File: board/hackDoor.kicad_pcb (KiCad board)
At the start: 2 copper layers, 66 x 34.5 mm, 11 parts, among them P1 RFID Reader, P2 Lock Button, P3 Lock/Unlock, P4 RFID Reader, P5 Lock Button, Q1 BSS138, SW1 SW_PUSH, U1 RFID-ID12

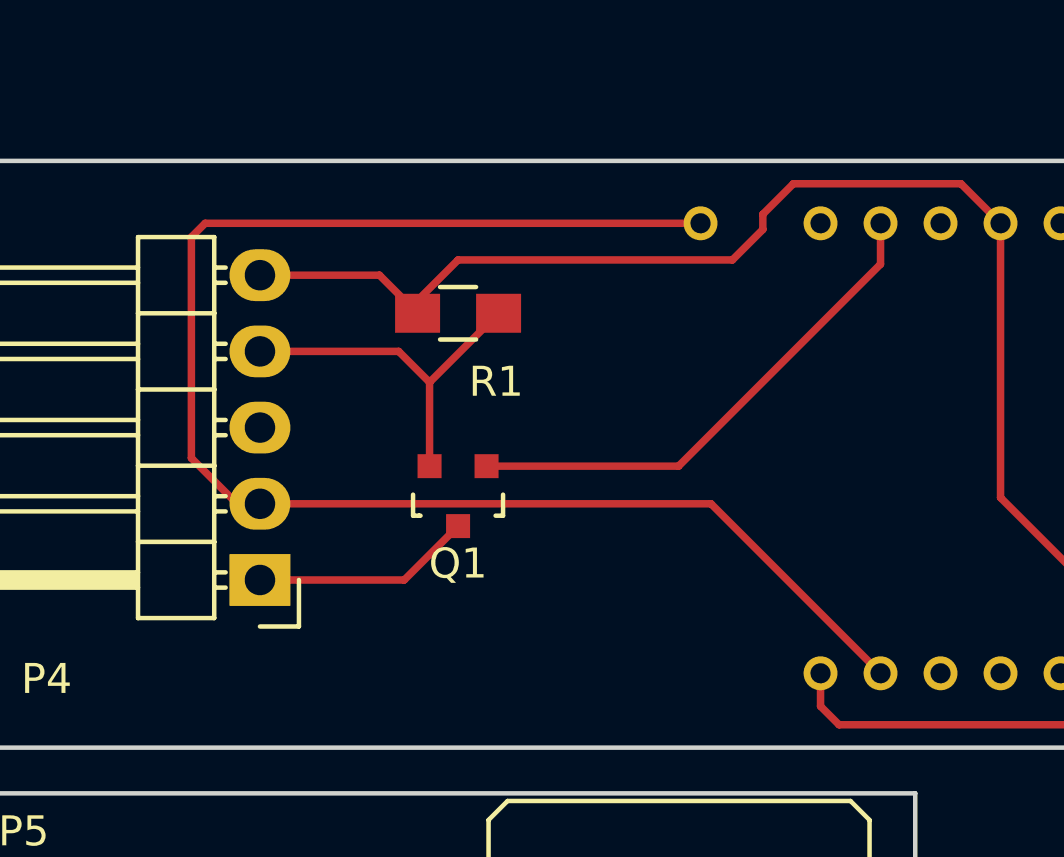
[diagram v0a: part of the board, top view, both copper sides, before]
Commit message: some routing changes for the board
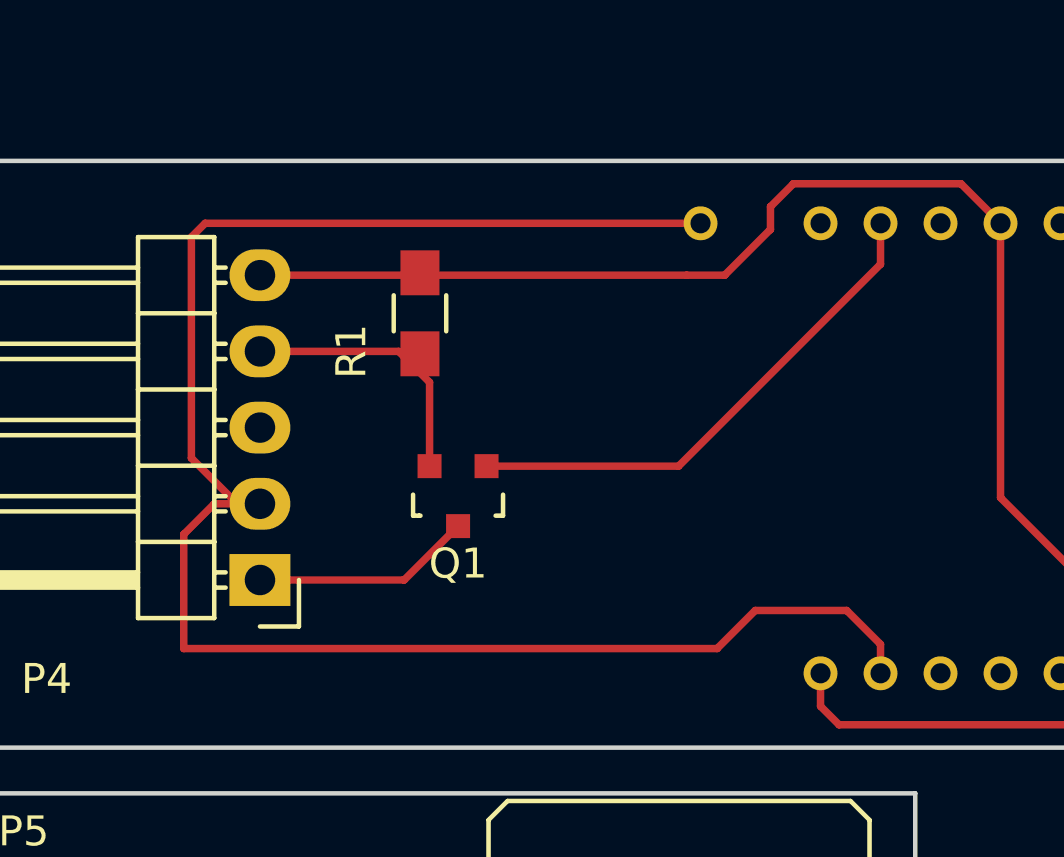
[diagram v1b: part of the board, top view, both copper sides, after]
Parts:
- moved R1 1.27 mm to (150.1, 96.5), turned to 90 degrees
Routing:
- net Net-(P4-Pad2): track 50.5 -> 59.4 mm
- net Net-(P4-Pad4): track 12.1 -> 8.88 mm
- net Net-(P4-Pad5): track 56.9 -> 55.7 mm
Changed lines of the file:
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@@
   (general
     (links 26)
-    (no_connects 3)
-    (area 109.144999 91.364999 130.123001 126.059001)
+    (no_connects 4)
+    (area 108.800862 87.247 175.335001 126.059001)
     (thickness 1.6)
     (drawings 14)
-    (tracks 70)
+    (tracks 73)
     (zones 0)
     (modules 11)
@@
   )
   (module Resistors_SMD:R_0805_HandSoldering (layer F.Cu)
-    (at 151.384 96.52 180)
+    (at 150.114 96.52 90)
     (descr "Resistor SMD 0805, hand soldering")
     (tags "resistor 0805")
     (attr smd)
-    (fp_text reference R1 (at -1.27 -2.286 180) (layer F.SilkS)
-      (effects (font (size 1 1) (thickness 0.15)))
-    )
-    (fp_text value 1k (at 0 2.1 180) (layer F.Fab)
+    (fp_text reference R1 (at -1.27 -2.286 90) (layer F.SilkS)
+      (effects (font (size 1 1) (thickness 0.15)))
+    )
+    (fp_text value 1k (at 0 2.1 90) (layer F.Fab)
       (effects (font (size 1 1) (thickness 0.15)))
     )
@@
     (fp_line (start 0.6 0.875) (end -0.6 0.875) (layer F.SilkS) (width 0.15))
     (fp_line (start -0.6 -0.875) (end 0.6 -0.875) (layer F.SilkS) (width 0.15))
-    (pad 1 smd rect (at -1.35 0 180) (size 1.5 1.3) (layers F.Cu F.Paste F.Mask)
+    (pad 1 smd rect (at -1.35 0 90) (size 1.5 1.3) (layers F.Cu F.Paste F.Mask)
       (net 11 "Net-(P4-Pad4)"))
-    (pad 2 smd rect (at 1.35 0 180) (size 1.5 1.3) (layers F.Cu F.Paste F.Mask)
+    (pad 2 smd rect (at 1.35 0 90) (size 1.5 1.3) (layers F.Cu F.Paste F.Mask)
       (net 12 "Net-(P4-Pad5)"))
     (model Resistors_SMD.3dshapes/R_0805_HandSoldering.wrl
@@
   (segment (start 149.404 97.79) (end 150.434 98.82) (width 0.25) (layer F.Cu) (net 11))
   (segment (start 150.434 101.61524) (end 150.434 98.82) (width 0.25) (layer F.Cu) (net 11))
-  (segment (start 150.434 98.82) (end 152.734 96.52) (width 0.25) (layer F.Cu) (net 11))
+  (segment (start 144.78 95.25) (end 150.034 95.25) (width 0.25) (layer F.Cu) (net 12) (status C00000))
+  (segment (start 150.034 95.25) (end 159.004 95.25) (width 0.25) (layer F.Cu) (net 12) (status 400000))
+  (segment (start 159.004 95.25) (end 160.274 95.25) (width 0.25) (layer F.Cu) (net 12))
+  (segment (start 160.274 95.25) (end 161.798 93.726) (width 0.25) (layer F.Cu) (net 12))
+  (segment (start 161.798 93.726) (end 161.798 92.964) (width 0.25) (layer F.Cu) (net 12))
+  (segment (start 161.798 92.964) (end 162.56 92.202) (width 0.25) (layer F.Cu) (net 12))
   (segment (start 162.56 92.202) (end 168.148 92.202) (width 0.25) (layer F.Cu) (net 12))
+  (segment (start 168.148 92.202) (end 169.466 93.52) (width 0.25) (layer F.Cu) (net 12) (status 800000))
   (segment (start 163.466 108.52) (end 163.466 109.618) (width 0.25) (layer F.Cu) (net 12))
   (segment (start 169.466 102.664) (end 169.466 93.52) (width 0.25) (layer F.Cu) (net 12))
@@
   (segment (start 164.084 110.236) (end 172.212 110.236) (width 0.25) (layer F.Cu) (net 12))
   (segment (start 163.466 109.618) (end 164.084 110.236) (width 0.25) (layer F.Cu) (net 12))
-  (segment (start 150.034 96.52) (end 150.034 96.092) (width 0.25) (layer F.Cu) (net 12))
-  (segment (start 150.034 96.092) (end 151.384 94.742) (width 0.25) (layer F.Cu) (net 12))
-  (segment (start 168.148 92.202) (end 169.466 93.52) (width 0.25) (layer F.Cu) (net 12))
-  (segment (start 161.544 93.218) (end 162.56 92.202) (width 0.25) (layer F.Cu) (net 12))
-  (segment (start 161.544 93.726) (end 161.544 93.218) (width 0.25) (layer F.Cu) (net 12))
-  (segment (start 160.528 94.742) (end 161.544 93.726) (width 0.25) (layer F.Cu) (net 12))
-  (segment (start 151.384 94.742) (end 160.528 94.742) (width 0.25) (layer F.Cu) (net 12))
-  (segment (start 144.78 95.25) (end 148.764 95.25) (width 0.25) (layer F.Cu) (net 12))
-  (segment (start 148.764 95.25) (end 150.034 96.52) (width 0.25) (layer F.Cu) (net 12))
   (segment (start 144.78 122.682) (end 149.272 122.682) (width 0.25) (layer F.Cu) (net 13))
   (segment (start 149.272 122.682) (end 149.606 123.016) (width 0.25) (layer F.Cu) (net 13))
@@
   (segment (start 158.73476 101.61524) (end 152.334 101.61524) (width 0.25) (layer F.Cu) (net 33))
   (segment (start 165.466 94.884) (end 158.73476 101.61524) (width 0.25) (layer F.Cu) (net 33))
+  (segment (start 144.78 102.87) (end 143.256 102.87) (width 0.25) (layer F.Cu) (net 34))
+  (segment (start 165.466 107.554) (end 165.466 108.52) (width 0.25) (layer F.Cu) (net 34))
+  (segment (start 164.338 106.426) (end 165.466 107.554) (width 0.25) (layer F.Cu) (net 34))
+  (segment (start 161.29 106.426) (end 164.338 106.426) (width 0.25) (layer F.Cu) (net 34))
+  (segment (start 160.02 107.696) (end 161.29 106.426) (width 0.25) (layer F.Cu) (net 34))
+  (segment (start 142.24 107.696) (end 160.02 107.696) (width 0.25) (layer F.Cu) (net 34))
+  (segment (start 142.24 103.886) (end 142.24 107.696) (width 0.25) (layer F.Cu) (net 34))
+  (segment (start 143.256 102.87) (end 142.24 103.886) (width 0.25) (layer F.Cu) (net 34))
   (segment (start 144.78 102.87) (end 144.018 102.87) (width 0.25) (layer F.Cu) (net 34))
   (segment (start 144.018 102.87) (end 142.494 101.346) (width 0.25) (layer F.Cu) (net 34))
@@
   (segment (start 142.494 93.98) (end 142.954 93.52) (width 0.25) (layer F.Cu) (net 34))
   (segment (start 142.494 101.346) (end 142.494 93.98) (width 0.25) (layer F.Cu) (net 34))
-  (segment (start 144.78 102.87) (end 159.816 102.87) (width 0.25) (layer F.Cu) (net 34))
-  (segment (start 159.816 102.87) (end 165.466 108.52) (width 0.25) (layer F.Cu) (net 34))
   (zone (net 5) (net_name GND) (layer F.Cu) (hatch edge 0.508)
     (connect_pads (clearance 0.508))

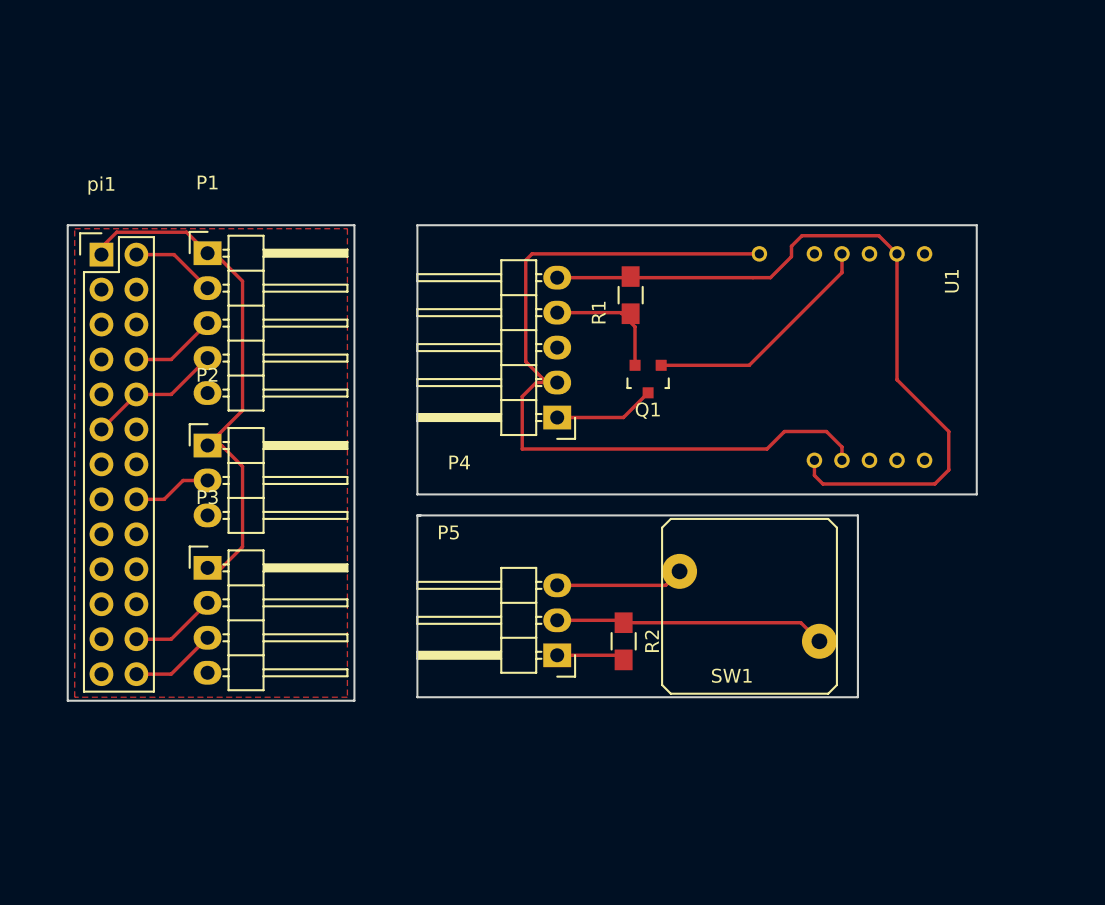
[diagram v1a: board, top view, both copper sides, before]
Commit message: changed trace width to .30 mm
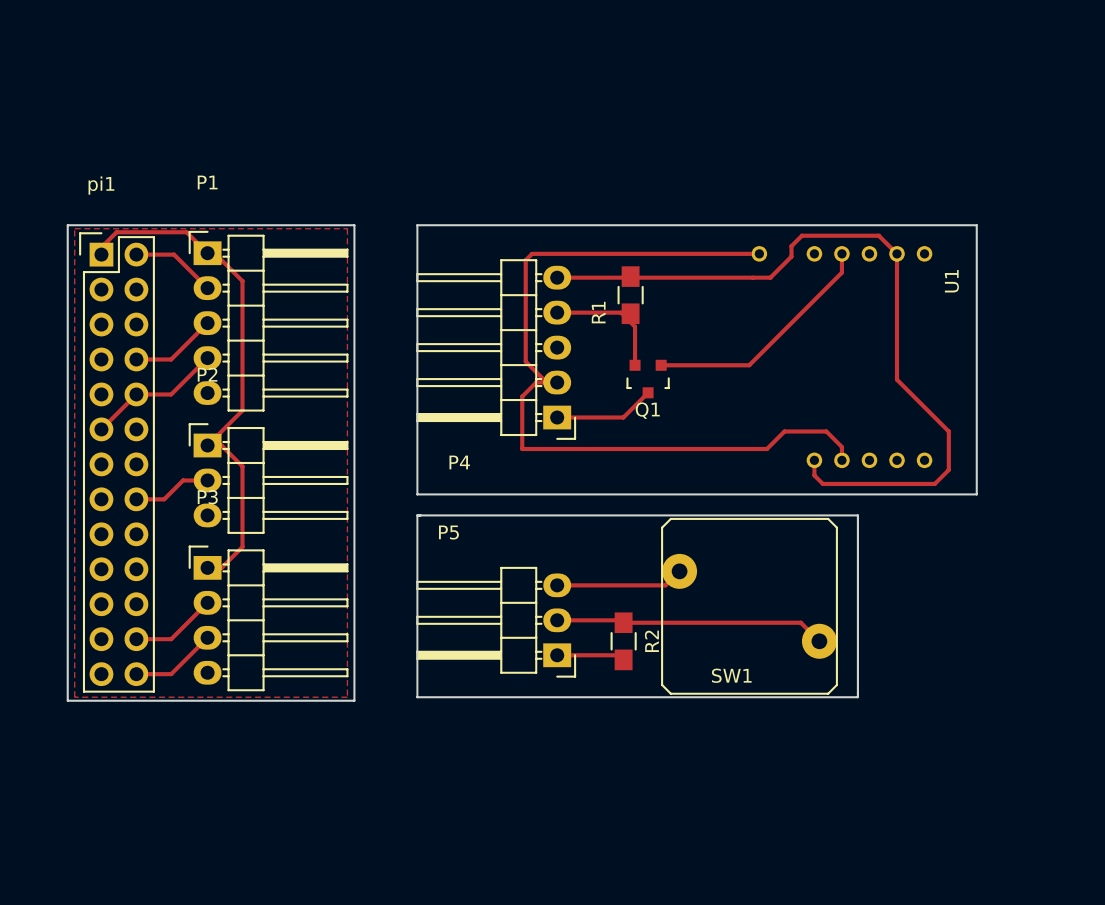
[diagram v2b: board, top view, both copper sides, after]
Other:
- net class Default: trace_width 0.25 -> 0.3

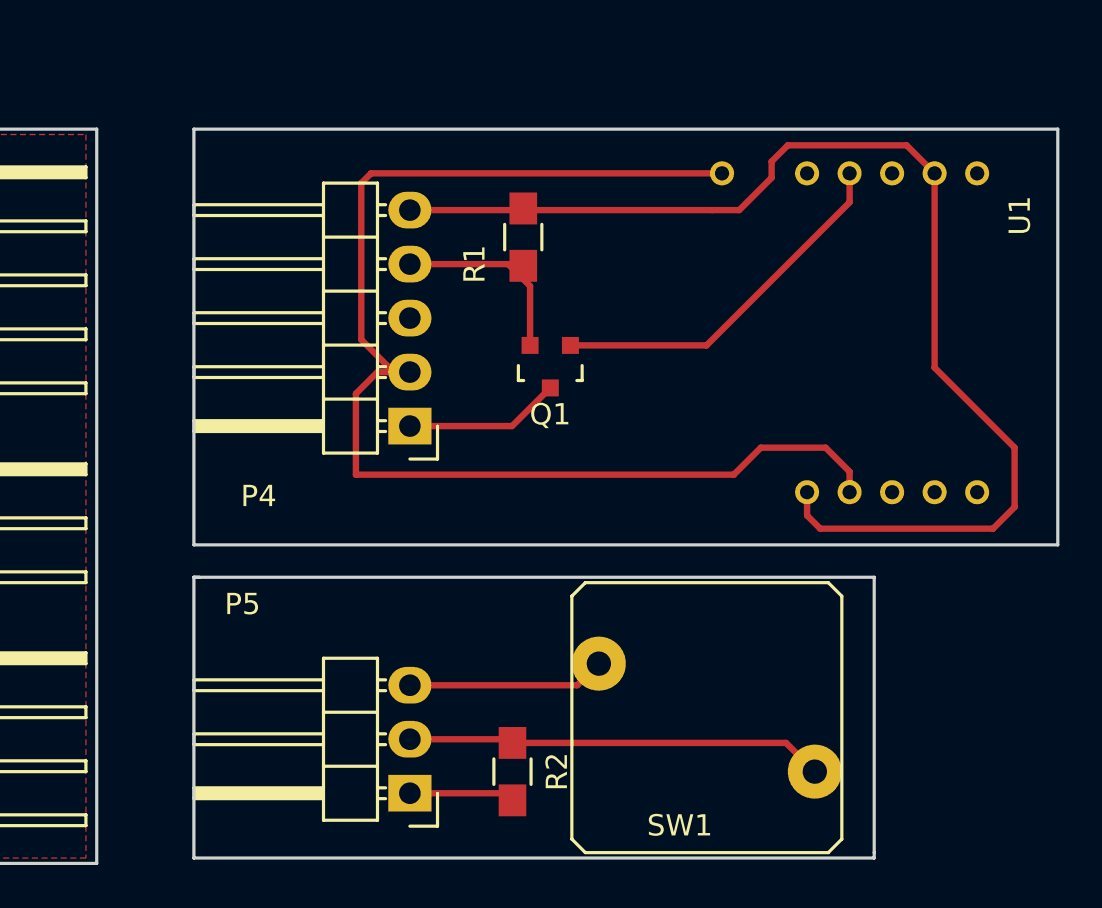
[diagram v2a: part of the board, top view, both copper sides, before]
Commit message: adding fabrication outputs
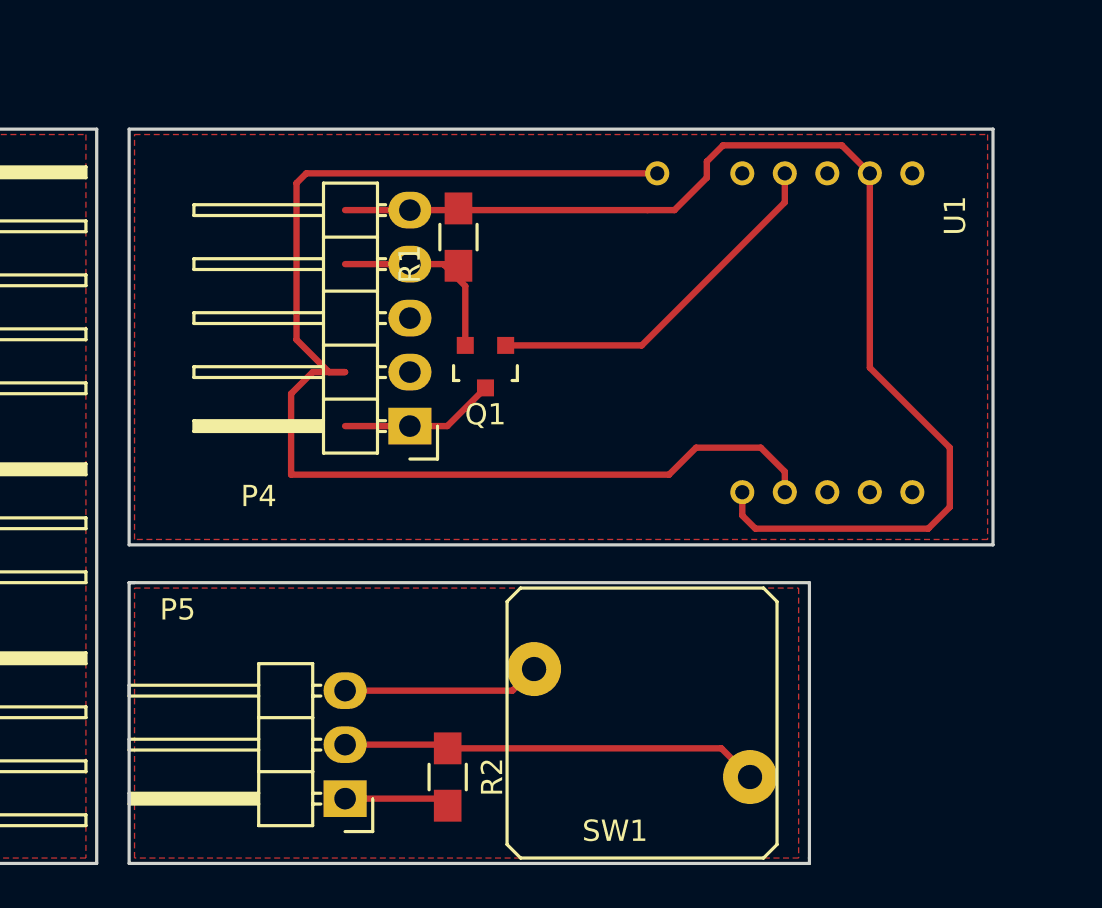
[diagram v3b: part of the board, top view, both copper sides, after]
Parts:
- moved P5 3.06 mm to (141.7, 122.9)
- moved R2 3.06 mm to (146.6, 121.9)
- moved SW1 3.06 mm to (155.7, 119.4)
- moved R1 3.05 mm to (147.1, 96.5)
- moved U1 3.05 mm to (169.4, 96.5)
- moved Q1 3.05 mm to (148.3, 102.6)
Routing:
- added copper zone on F.Cu, net Net-(P4-Pad5)
- added copper zone on F.Cu, net Net-(P5-Pad3)
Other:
- board size 66 x 34.5 mm -> 63 x 34.5 mm
